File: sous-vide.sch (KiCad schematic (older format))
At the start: 29 parts, among them J1 Heater, J2 Power, J3 Conn_01x02, J4 Jumper, J5 Jumper, Q1 2N3904, SW1 SW_Push_Dual, SW2 SW_Push_Dual, U1 G5LE, U2 RAC01, U3 node_mcu1.0, U4 P090S, U5 LCD_Backpack

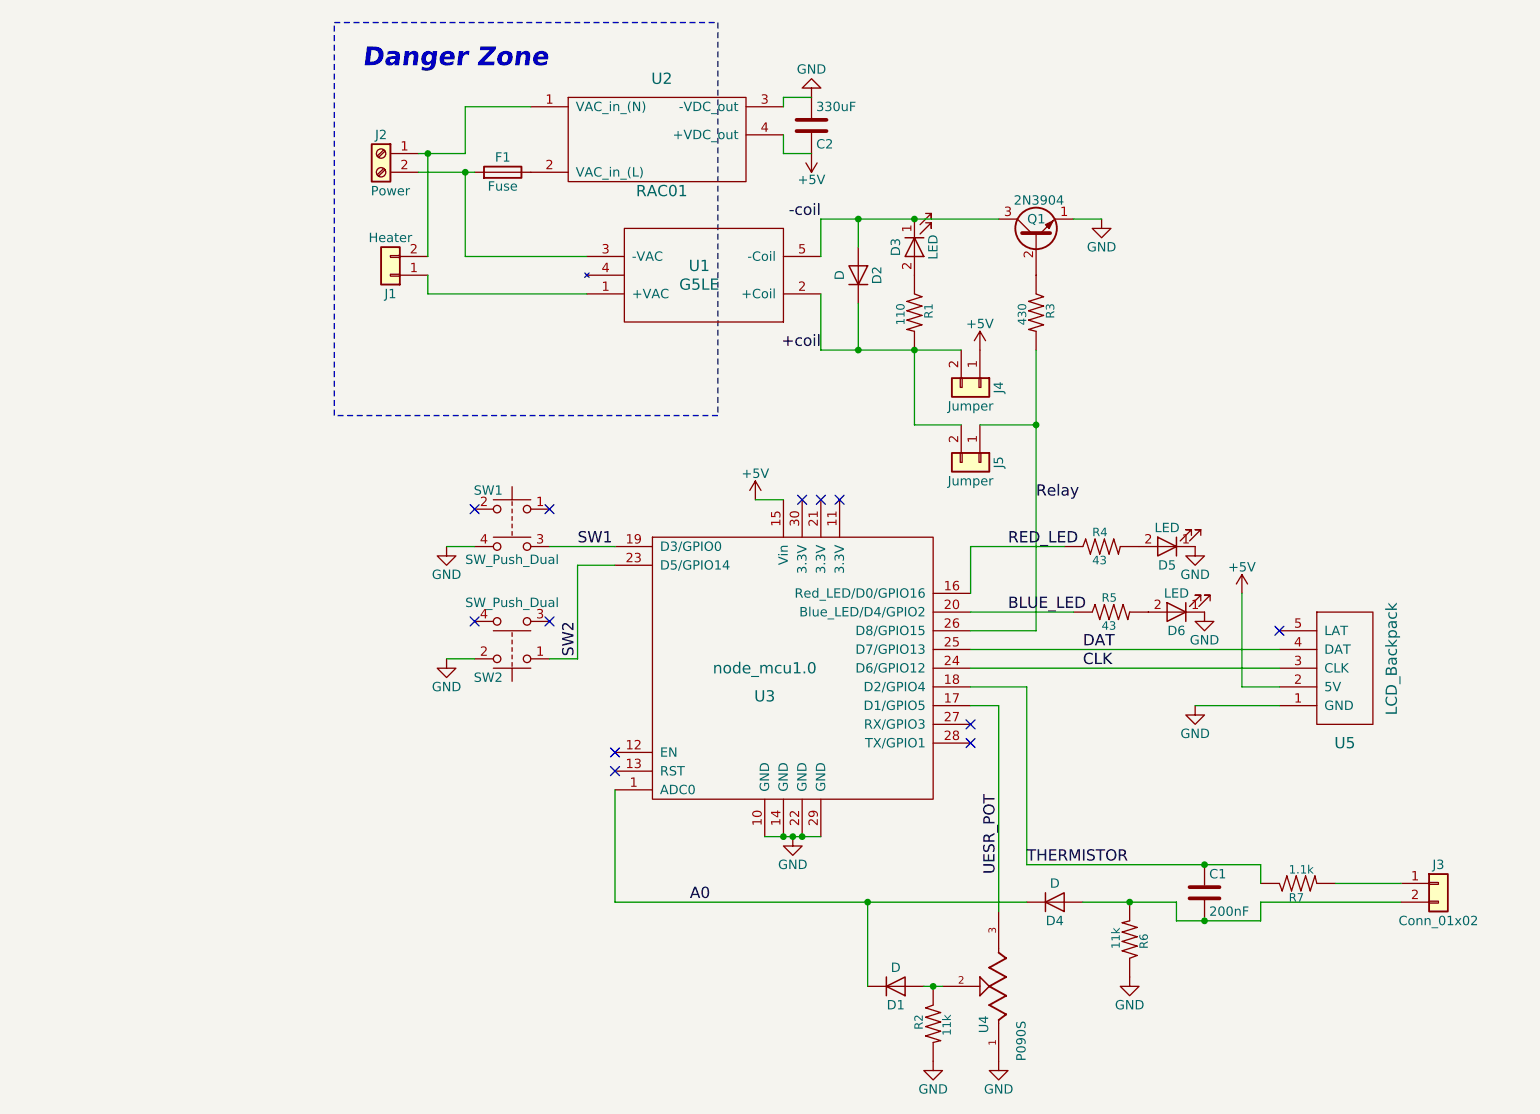
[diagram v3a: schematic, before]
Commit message: new schematic using NC7SB analog multiplexer
 - requires surface mount :(
 - re-annotated everything so routing will be very annoying

Also, I was testing to see why/how relay load affected analog readings
and I discovered a few odd things:

 - D4/GPIO2/Blue_LED does not light up. low voltage?
 - using a transistor on *just* the pot (instead of GPIO directly)
 seemed to remove effect of relay
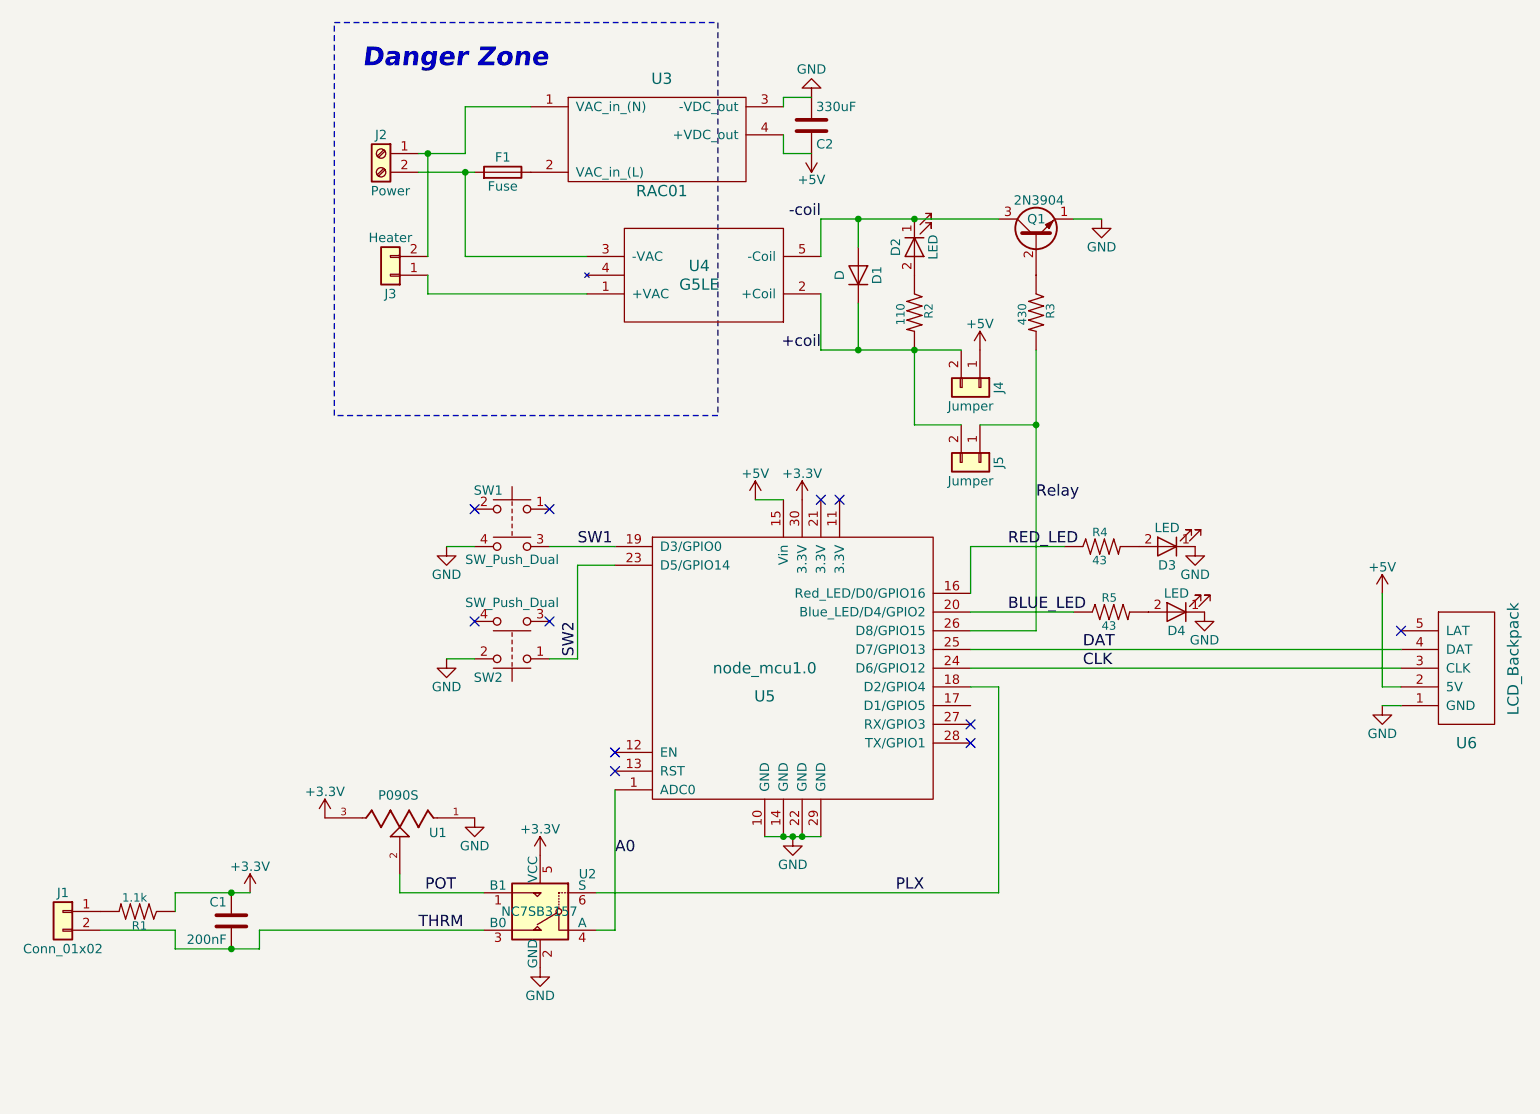
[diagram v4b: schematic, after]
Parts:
- removed D1, D4: D, Diodes_THT:D_DO-35_SOD27_P7.62mm_Horizontal, symbol D
- removed R2, R6: 11k, Resistors_THT:R_Axial_DIN0207_L6.3mm_D2.5mm_P10.16mm_Horizontal, symbol RESISTOR0402
- added U2: NC7SB3157, symbol NC7SB3157
- renumbered D2 to D1, D3 to D2, D5 to D3, D6 to D4, J3 to J1, J1 to J3, R7 to R1, R1 to R2, U4 to U1, U2 to U3, U1 to U4, U3 to U5, U5 to U6
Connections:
- net A0: now also U2.4 (A)
- net GND: now also U2.2 (GND)
- net POT: now reaches U1.2 (S)
- net POT: now also U2.1 (B1)
- net +3V3: now reaches U5.30 (3.3V)
- net +3V3: now also C1.1, R1.1, U1.3 (CW), U2.5 (VCC)
- net THRM: now reaches C1.2, J1.2 (Pin_2)
- net THRM: now also U2.3 (B0)
- removed net THERMISTOR: C1.1, R1.1, U5.18 (D2/GPIO4)
- net UESR_POT: no longer names the net of U5.17 (D1/GPIO5)
- net UESR_POT: no longer U1.3 (CW)
- new net PLX: U2.6 (S), U5.18 (D2/GPIO4)
- no-connect marks 12 -> 11
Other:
- moved on the sheet: C1, J1, R1, U1, U6

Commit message: reverted to dio multiplexor because it works
 - measure 67mA on the coil, 5.31mA on the DIO
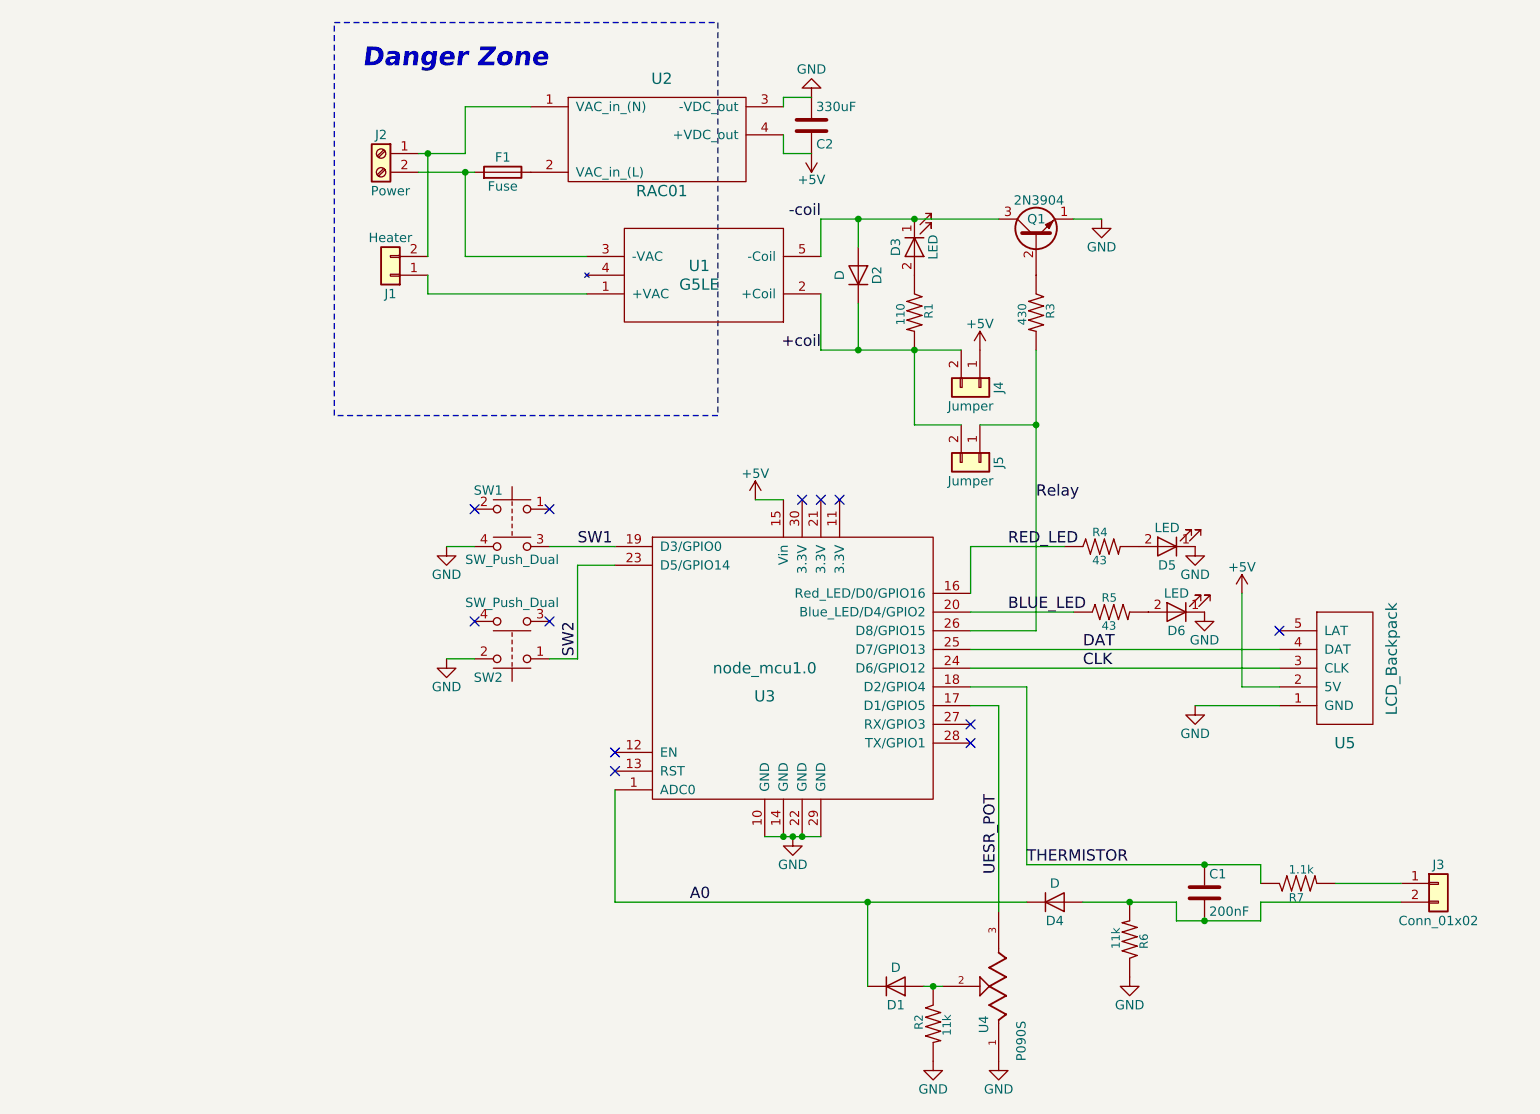
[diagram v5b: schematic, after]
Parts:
- removed U2: NC7SB3157, symbol NC7SB3157
- added D1, D4: D, Diodes_THT:D_DO-35_SOD27_P7.62mm_Horizontal, symbol D
- added R2, R6: 11k, Resistors_THT:R_Axial_DIN0207_L6.3mm_D2.5mm_P10.16mm_Horizontal, symbol RESISTOR0402
- renumbered D1 to D2, D2 to D3, D3 to D5, D4 to D6, J3 to J1, J1 to J3, R2 to R1, R1 to R7, U4 to U1, U3 to U2, U5 to U3, U1 to U4, U6 to U5
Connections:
- net PLX is gone; now on net THERMISTOR: U3.18 (D2/GPIO4)
- net A0: now also D1.1 (K), D4.1 (K)
- net GND: now also R2.2, R6.1
- net UESR_POT: now reaches U3.17 (D1/GPIO5)
- net UESR_POT: now also U4.3 (CW)
- net +3V3 renamed THERMISTOR
- net THERMISTOR: no longer U3.30 (3.3V), U4.3 (CW)
- net POT: no longer names the net of U4.2 (S)
- net POT: now also D1.2 (A), R2.1
- net THRM: no longer names the net of C1.2, J3.2 (Pin_2)
- net THRM: now also D4.2 (A), R6.2
- no-connect marks 11 -> 12
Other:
- moved on the sheet: C1, J3, R7, U4, U5
